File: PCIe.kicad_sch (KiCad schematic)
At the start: 1 part, among them J12 10018783-11200TLF

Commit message: library management
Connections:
- net +12v: no longer names the net of J12.B1 (+12v), J12.B2 (+12v), J12.B3 (+12v)
- net +12v: no longer J12.A2 (+12V), J12.A3 (+12V)
- new net: J12.A2 (+12V), J12.A3 (+12V)
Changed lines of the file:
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@@
   (junction (at 130.81 71.12) (diameter 1.016) (color 0 0 0 0))
   (junction (at 130.81 76.2) (diameter 1.016) (color 0 0 0 0))
-  (junction (at 132.08 33.02) (diameter 1.016) (color 0 0 0 0))
   (junction (at 132.08 35.56) (diameter 1.016) (color 0 0 0 0))
   (junction (at 161.29 35.56) (diameter 1.016) (color 0 0 0 0))
@@
   (no_connect (at 161.29 33.02))
   (no_connect (at 132.08 43.18))
-  (wire (pts (xy 117.475 33.02) (xy 132.08 33.02))
-    (stroke (width 0) (type solid) (color 0 0 0 0))
-  )
   (wire (pts (xy 118.11 50.8) (xy 129.54 50.8))
     (stroke (width 0) (type solid) (color 0 0 0 0))
@@
     (effects (font (size 1.27 1.27)) (justify right bottom))
   )
-  (label "+12v" (at 120.65 33.02 0)
-    (effects (font (size 1.27 1.27)) (justify left bottom))
-  )
   (label "+3.3v" (at 120.65 50.8 0)
-    (effects (font (size 1.27 1.27)) (justify left bottom))
-  )
-  (label "+12v" (at 166.37 35.56 0)
     (effects (font (size 1.27 1.27)) (justify left bottom))
   )
@@
     (effects (font (size 1.27 1.27)) (justify right))
   )
-  (hierarchical_label "+12v" (shape input) (at 117.475 33.02 180)
-    (effects (font (size 1.27 1.27)) (justify right))
-  )

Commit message: updating readme and some layout
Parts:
- added J?: 2199119-4, TE_2199119-4, symbol 2199119-4:2199119-4
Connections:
- new net: J?.SH1 (SHIELD), J?.SH2 (SHIELD)
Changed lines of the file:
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@@
   (junction (at 165.1 50.8) (diameter 1.016) (color 0 0 0 0))
   (junction (at 165.1 53.34) (diameter 1.016) (color 0 0 0 0))
-  (no_connect (at 161.29 48.26))
-  (no_connect (at 132.08 43.18))
-  (no_connect (at 132.08 58.42))
   (no_connect (at 161.29 33.02))
   (no_connect (at 132.08 73.66))
+  (no_connect (at 132.08 43.18))
+  (no_connect (at 161.29 48.26))
+  (no_connect (at 132.08 58.42))
   (no_connect (at 132.08 45.72))
   (wire (pts (xy 118.11 50.8) (xy 129.54 50.8))
@@
     )
   )
+  (symbol (lib_id "2199119-4:2199119-4") (at 243.84 93.98 0) (unit 1)
+    (in_bom yes) (on_board yes)
+    (property "Reference" "J?" (id 0) (at 244.475 40.64 0))
+    (property "Value" "2199119-4" (id 1) (at 244.475 43.18 0))
+    (property "Footprint" "TE_2199119-4" (id 2) (at 243.84 93.98 0)
+      (effects (font (size 1.27 1.27)) (justify left bottom) hide)
+    )
+    (property "Datasheet" "" (id 3) (at 243.84 93.98 0)
+      (effects (font (size 1.27 1.27)) (justify left bottom) hide)
+    )
+    (property "Comment" "2199119-4" (id 4) (at 243.84 93.98 0)
+      (effects (font (size 1.27 1.27)) (justify left bottom) hide)
+    )
+  )

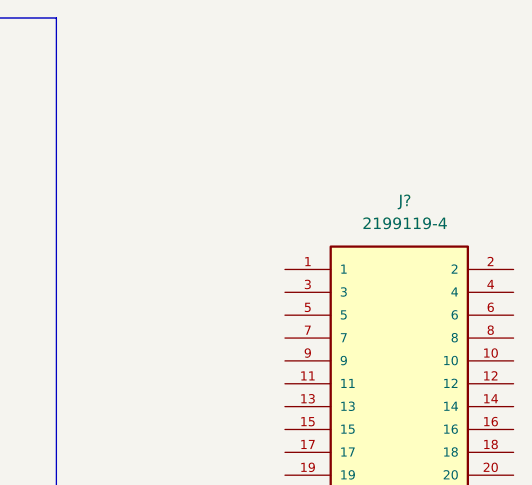
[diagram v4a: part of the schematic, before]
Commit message: started routing USB, added usb power switches, routing some USB-C
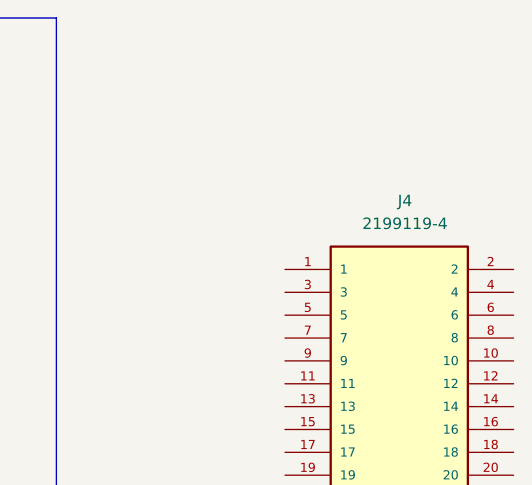
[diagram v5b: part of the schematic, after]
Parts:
- gave numbers to parts that had none: 1
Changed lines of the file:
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@@
   (junction (at 165.1 50.8) (diameter 1.016) (color 0 0 0 0))
   (junction (at 165.1 53.34) (diameter 1.016) (color 0 0 0 0))
-  (no_connect (at 161.29 33.02))
   (no_connect (at 132.08 73.66))
   (no_connect (at 132.08 43.18))
   (no_connect (at 161.29 48.26))
+  (no_connect (at 132.08 45.72))
+  (no_connect (at 161.29 33.02))
   (no_connect (at 132.08 58.42))
-  (no_connect (at 132.08 45.72))
   (wire (pts (xy 118.11 50.8) (xy 129.54 50.8))
     (stroke (width 0) (type solid) (color 0 0 0 0))
@@
   (symbol (lib_id "2199119-4:2199119-4") (at 243.84 93.98 0) (unit 1)
     (in_bom yes) (on_board yes)
-    (property "Reference" "J?" (id 0) (at 244.475 40.64 0))
+    (property "Reference" "J4" (id 0) (at 244.475 40.64 0))
     (property "Value" "2199119-4" (id 1) (at 244.475 43.18 0))
     (property "Footprint" "TE_2199119-4" (id 2) (at 243.84 93.98 0)
